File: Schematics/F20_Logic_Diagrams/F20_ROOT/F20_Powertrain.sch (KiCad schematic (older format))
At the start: 1 part, among them U1 Fan

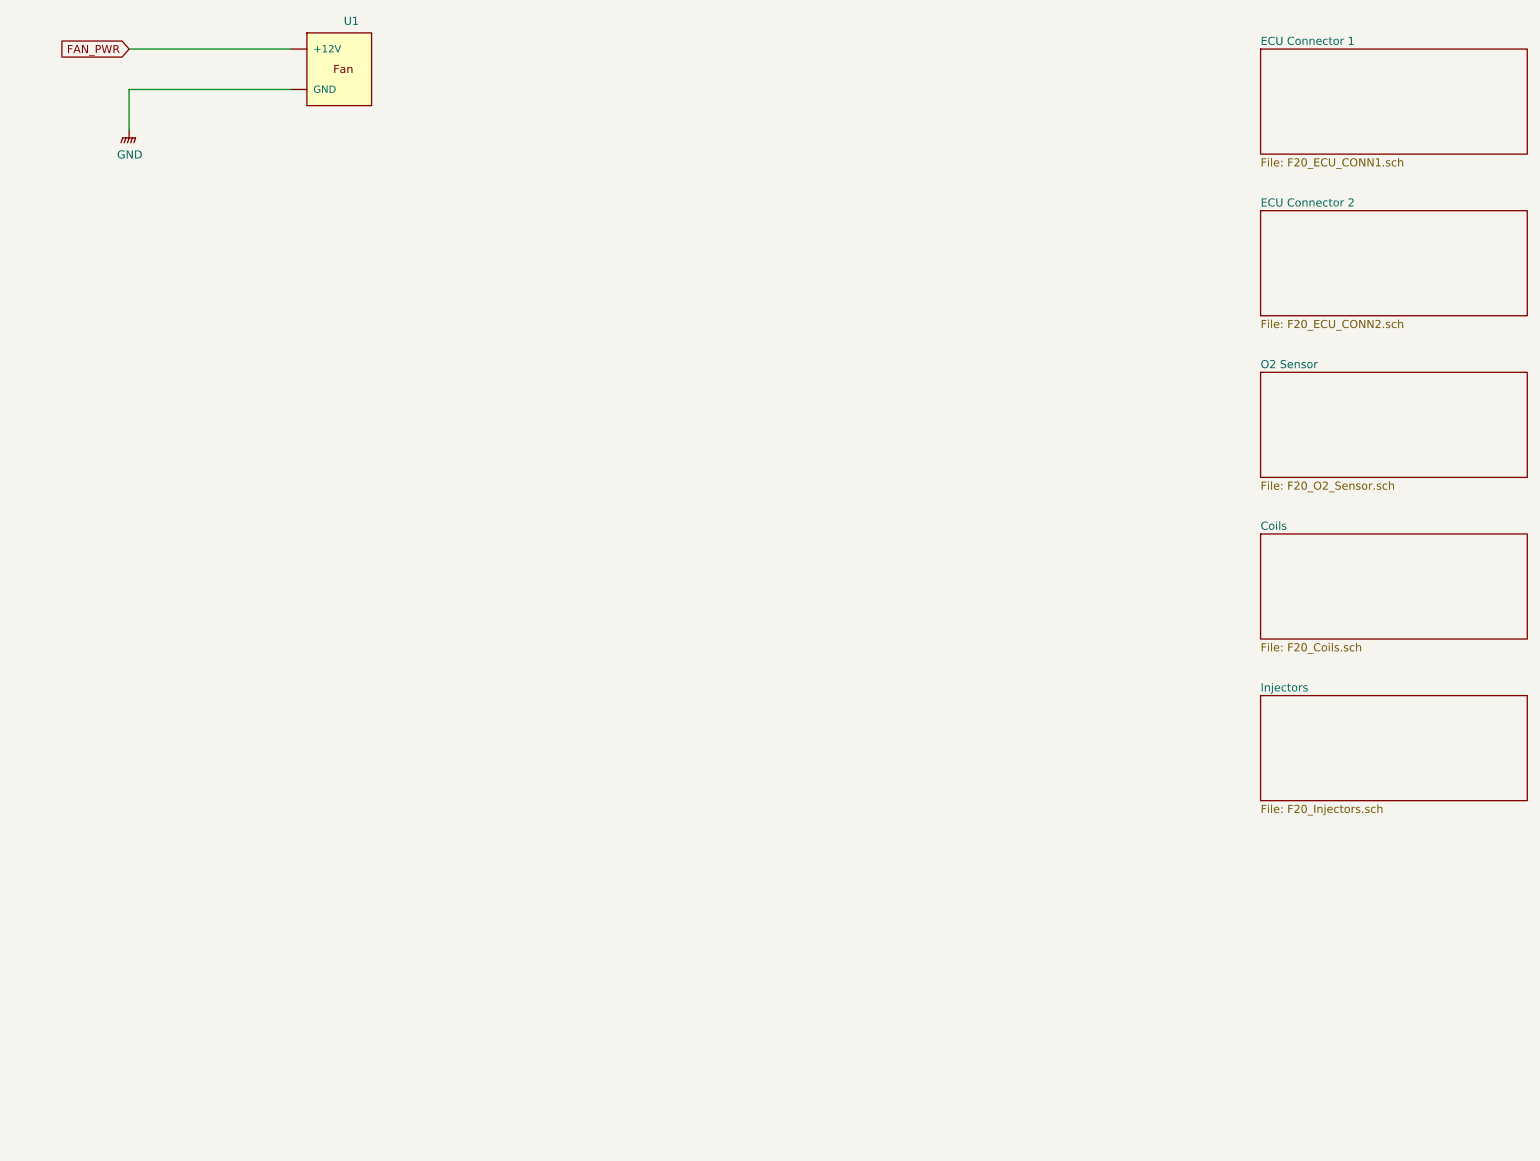
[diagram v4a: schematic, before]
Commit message: Major powertrain update, added shifting schematic
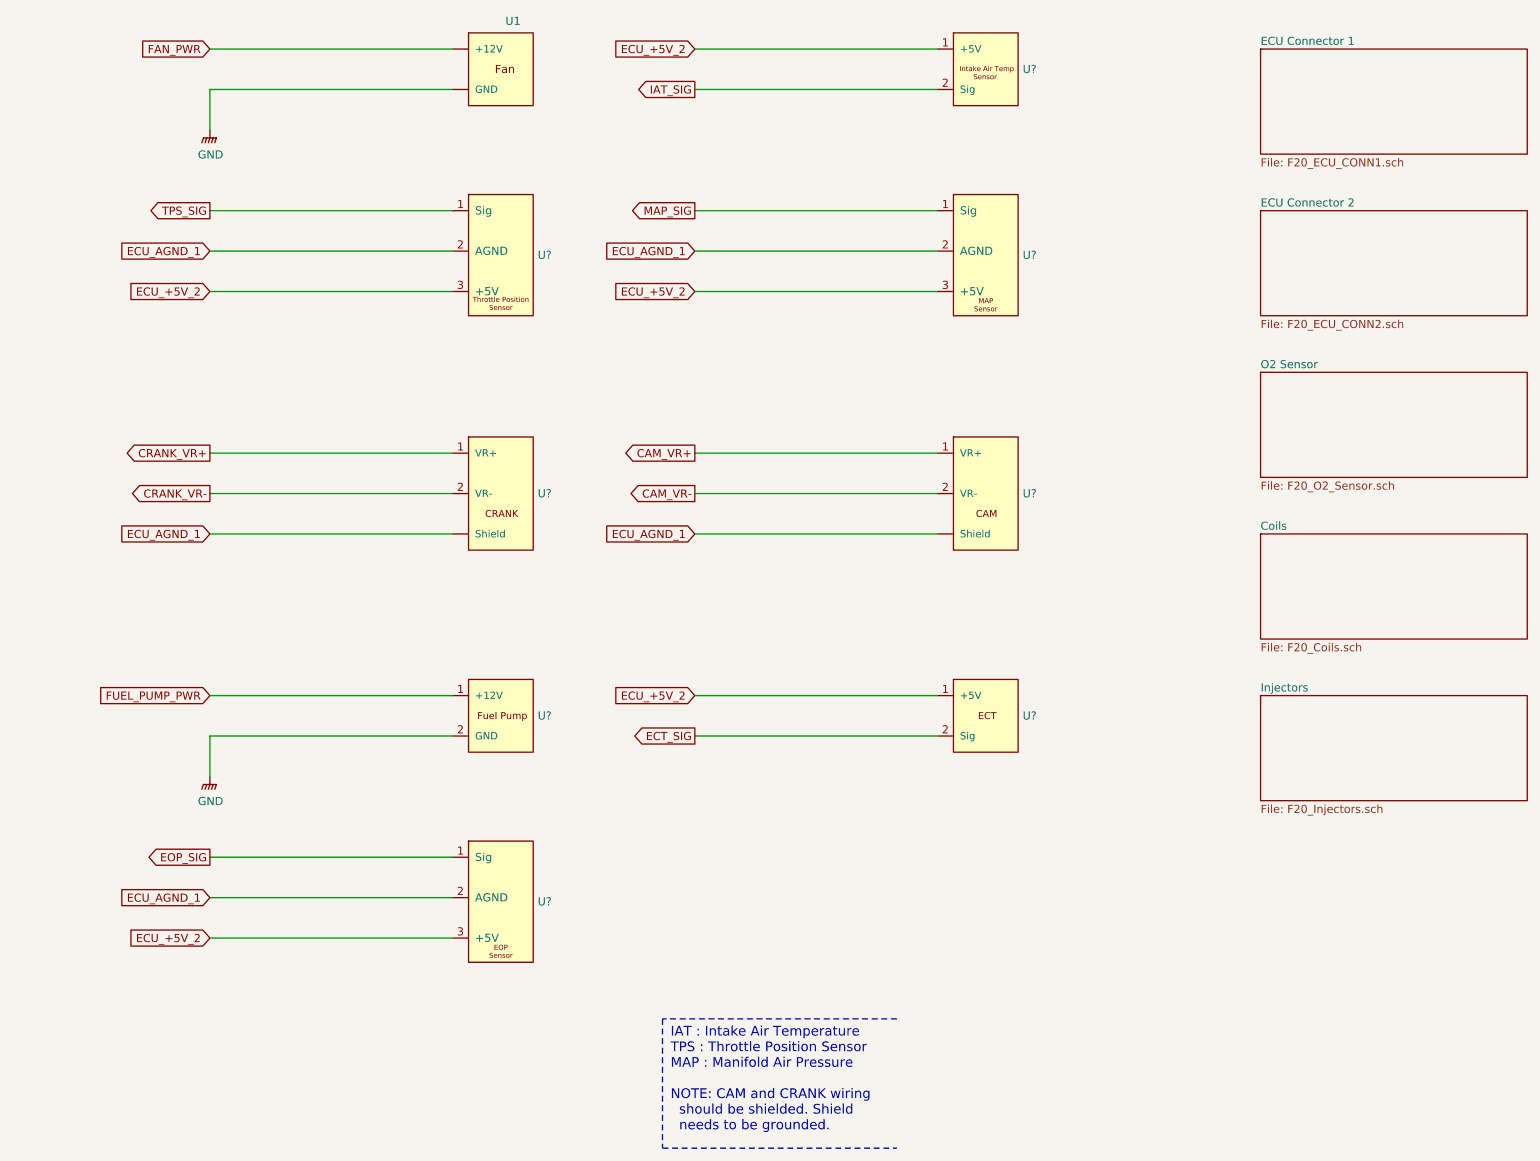
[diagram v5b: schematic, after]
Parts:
- added U?: Fuel_Pump, symbol FSAE_Library:Fuel_Pump
- added U?: Intake_Air_Temp, symbol FSAE_Library:Intake_Air_Temp
- added U?: Throttle_Position_Sensor, symbol FSAE_Library:Throttle_Position_Sensor
- added U?: MAP_Sensor, symbol FSAE_Library:MAP_Sensor
- added U?: Camshaft_Sensor, symbol FSAE_Library:Camshaft_Sensor
- added U?: Crankshaft_Sensor, symbol FSAE_Library:Crankshaft_Sensor
- added U?: ECT_Sensor, symbol FSAE_Library:ECT_Sensor
- added U?: EOP_Sensor, symbol FSAE_Library:EOP_Sensor
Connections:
- net GNDPWR: now also U?.2 (GND)
- new net CAM_VR+: U?.1 (VR+)
- new net CAM_VR-: U?.2 (VR-)
- new net CRANK_VR+: U?.1 (VR+)
- new net CRANK_VR-: U?.2 (VR-)
- new net ECT_SIG: U?.2 (Sig)
- new net ECU_+5V_2: U?.1 (+5V), U?.1 (+5V), U?.3 (+5V), U?.3 (+5V), U?.3 (+5V)
- new net ECU_AGND_1: U?.2 (AGND), U?.2 (AGND), U?.2 (AGND), U?.~ (Shield), U?.~ (Shield)
- new net EOP_SIG: U?.1 (Sig)
- new net FUEL_PUMP_PWR: U?.1 (+12V)
- new net IAT_SIG: U?.2 (Sig)
- new net MAP_SIG: U?.1 (Sig)
- new net TPS_SIG: U?.1 (Sig)
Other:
- note added: "IAT : Intake Air Temperature\nTPS : Throttle Position Sensor\nMAP : Manifold Air Pressure\n\nNOTE: CAM and CRANK wiring\n should be shielded. Shield\n needs to be grounded."
- moved on the sheet: U1
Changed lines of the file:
@@
 $Descr A 11000 8500
 encoding utf-8
-Sheet 2 14
+Sheet 2 15
 Title "Engine"
-Date "2020-02-03"
+Date "2020-03-03"
 Rev "A"
 Comp "F20"
-Comment1 "Cristian Valadez"
+Comment1 "Cristian Valadez, Alex Domagala"
 Comment2 ""
 Comment3 ""
@@
 L FSAE_Library:Fan U1
 U 1 1 5E3D2712
-P 2500 1000
-F 0 "U1" H 2875 1173 50  0000 C CNN
-F 1 "Fan" H 2750 1150 50  0001 C CNN
-F 2 "" H 3000 1500 50  0001 C CNN
-F 3 "" H 3000 1500 50  0001 C CNN
-	1    2500 1000
+P 3500 1000
+F 0 "U1" H 3875 1173 50  0000 C CNN
+F 1 "Fan" H 3750 1150 50  0001 C CNN
+F 2 "" H 4000 1500 50  0001 C CNN
+F 3 "" H 4000 1500 50  0001 C CNN
+	1    3500 1000
 	1    0    0    -1
 $EndComp
@@
 L FSAE_Library:GND #PWR01
 U 1 1 5E3D3AE8
-P 1500 1500
-F 0 "#PWR01" H 1500 1300 50  0001 C CNN
-F 1 "GND" H 1504 1346 50  0000 C CNN
-F 2 "" H 1500 1450 50  0001 C CNN
-F 3 "" H 1500 1450 50  0001 C CNN
-	1    1500 1500
-	1    0    0    -1
-$EndComp
-Wire Wire Line
-	1500 1500 1500 1250
-Wire Wire Line
-	1500 1250 2500 1250
-Text GLabel 1500 1000 0    50   Input ~ 0
+P 2000 1500
+F 0 "#PWR01" H 2000 1300 50  0001 C CNN
+F 1 "GND" H 2004 1346 50  0000 C CNN
+F 2 "" H 2000 1450 50  0001 C CNN
+F 3 "" H 2000 1450 50  0001 C CNN
+	1    2000 1500
+	1    0    0    -1
+$EndComp
+Wire Wire Line
+	2000 1500 2000 1250
+Wire Wire Line
+	2000 1250 3500 1250
+Text GLabel 2000 1000 0    50   Input ~ 0
 FAN_PWR
 Wire Wire Line
-	1500 1000 2500 1000
+	2000 1000 3500 1000
 $Sheet
 S 8500 3000 1650 650
@@
 F1 "F20_Injectors.sch" 50
 $EndSheet
+$Comp
+L FSAE_Library:Fuel_Pump U?
+U 1 1 5E5FB918
+P 3500 5000
+AR Path="/5E5F0904/5E5FB918" Ref="U?"  Part="1"
+AR Path="/5E1D1B45/5E5FB918" Ref="U?"  Part="1"
+F 0 "U?" H 4028 4875 50  0000 L CNN
+F 1 "Fuel_Pump" H 3750 5150 50  0001 C CNN
+F 2 "" H 4000 5500 50  0001 C CNN
+F 3 "" H 4000 5500 50  0001 C CNN
+	1    3500 5000
+	1    0    0    -1
+$EndComp
+Wire Wire Line
+	3500 5000 2000 5000
+Wire Wire Line
+	3500 5250 2000 5250
+Wire Wire Line
+	2000 5250 2000 5500
+$Comp
+L FSAE_Library:GND #PWR?
+U 1 1 5E5FB922
+P 2000 5500
+AR Path="/5E5F0904/5E5FB922" Ref="#PWR?"  Part="1"
+AR Path="/5E1D1B45/5E5FB922" Ref="#PWR?"  Part="1"
+F 0 "#PWR?" H 2000 5300 50  0001 C CNN
+F 1 "GND" H 2004 5346 50  0000 C CNN
+F 2 "" H 2000 5450 50  0001 C CNN
+F 3 "" H 2000 5450 50  0001 C CNN
+	1    2000 5500
+	1    0    0    -1
+$EndComp
+$Comp
+L FSAE_Library:Intake_Air_Temp U?
+U 1 1 5E5FB938
+P 6500 1000
+AR Path="/5E5F0904/5E5FB938" Ref="U?"  Part="1"
+AR Path="/5E1D1B45/5E5FB938" Ref="U?"  Part="1"
+F 0 "U?" H 7028 875 50  0000 L CNN
+F 1 "Intake_Air_Temp" H 6750 1150 50  0001 C CNN
+F 2 "" H 7000 1500 50  0001 C CNN
+F 3 "" H 7000 1500 50  0001 C CNN
+	1    6500 1000
+	1    0    0    -1
+$EndComp
+Wire Wire Line
+	6500 1000 5000 1000
+Wire Wire Line
+	6500 1250 5000 1250
+Text GLabel 5000 1250 0    50   Output ~ 0
+IAT_SIG
+$Comp
+L FSAE_Library:Throttle_Position_Sensor U?
+U 1 1 5E5FB942
+P 3500 2000
+AR Path="/5E5F0904/5E5FB942" Ref="U?"  Part="1"
+AR Path="/5E1D1B45/5E5FB942" Ref="U?"  Part="1"
+F 0 "U?" H 4028 1725 50  0000 L CNN
+F 1 "Throttle_Position_Sensor" H 3800 2150 50  0001 C CNN
+F 2 "" H 4000 2500 50  0001 C CNN
+F 3 "" H 4000 2500 50  0001 C CNN
+	1    3500 2000
+	1    0    0    -1
+$EndComp
+Text GLabel 2000 2500 0    50   Input ~ 0
+ECU_+5V_2
+Wire Wire Line
+	3500 2500 2000 2500
+Wire Wire Line
+	3500 2250 2000 2250
+Text GLabel 2000 2250 0    50   Input ~ 0
+ECU_AGND_1
+Wire Wire Line
+	3500 2000 2000 2000
+Text GLabel 2000 2000 0    50   Output ~ 0
+TPS_SIG
+$Comp
+L FSAE_Library:MAP_Sensor U?
+U 1 1 5E5FB94E
+P 6500 2000
+AR Path="/5E5F0904/5E5FB94E" Ref="U?"  Part="1"
+AR Path="/5E1D1B45/5E5FB94E" Ref="U?"  Part="1"
+F 0 "U?" H 7028 1725 50  0000 L CNN
+F 1 "MAP_Sensor" H 6800 2150 50  0001 C CNN
+F 2 "" H 7000 2500 50  0001 C CNN
+F 3 "" H 7000 2500 50  0001 C CNN
+	1    6500 2000
+	1    0    0    -1
+$EndComp
+Wire Wire Line
+	6500 2000 5000 2000
+Wire Wire Line
+	6500 2250 5000 2250
+Wire Wire Line
+	6500 2500 5000 2500
+Text GLabel 5000 2000 0    50   Output ~ 0
+MAP_SIG
+Text GLabel 5000 2250 0    50   Input ~ 0
+ECU_AGND_1
+Text GLabel 5000 2500 0    50   Input ~ 0
+ECU_+5V_2
+Wire Wire Line
+	3500 3500 2000 3500
+Wire Wire Line
+	3500 4000 2000 4000
+Text GLabel 5000 1000 0    50   Input ~ 0
+ECU_+5V_2
+Text Notes 4850 7700 0    60   ~ 0
+IAT : Intake Air Temperature\nTPS : Throttle Position Sensor\nMAP : Manifold Air Pressure\n\nNOTE: CAM and CRANK wiring\n  should be shielded. Shield\n  needs to be grounded.
+Text GLabel 2000 5000 0    50   Input ~ 0
+FUEL_PUMP_PWR
+Wire Wire Line
+	5000 4000 6500 4000
+Wire Wire Line
+	5000 3500 6500 3500
+Text GLabel 2000 3500 0    50   Output ~ 0
+CRANK_VR+
+Text GLabel 5000 3500 0    50   Output ~ 0
+CAM_VR+
+Wire Notes Line
+	6250 7000 4800 7000
+Wire Notes Line
+	4800 7000 4800 7800
+Wire Notes Line
+	4800 7800 6250 7800
+Text GLabel 2000 4000 0    50   Input ~ 0
+ECU_AGND_1
+Text GLabel 5000 4000 0    50   Input ~ 0
+ECU_AGND_1
+Wire Wire Line
+	3500 3750 2000 3750
+Text GLabel 2000 3750 0    50   Output ~ 0
+CRANK_VR-
+Wire Wire Line
+	6500 3750 5000 3750
+Text GLabel 5000 3750 0    50   Output ~ 0
+CAM_VR-
+$Comp
+L FSAE_Library:Camshaft_Sensor U?
+U 1 1 5E665C35
+P 6500 3500
+F 0 "U?" H 7028 3250 50  0000 L CNN
+F 1 "Camshaft_Sensor" H 6750 3650 50  0001 C CNN
+F 2 "" H 7000 4000 50  0001 C CNN
+F 3 "" H 7000 4000 50  0001 C CNN
+	1    6500 3500
+	1    0    0    -1
+$EndComp
+$Comp
+L FSAE_Library:Crankshaft_Sensor U?
+U 1 1 5E6666BD
+P 3500 3500
+F 0 "U?" H 4028 3250 50  0000 L CNN
+F 1 "Crankshaft_Sensor" H 3750 3650 50  0001 C CNN
+F 2 "" H 4000 4000 50  0001 C CNN
+F 3 "" H 4000 4000 50  0001 C CNN
+	1    3500 3500
+	1    0    0    -1
+$EndComp
+Text GLabel 5000 5250 0    50   Output ~ 0
+ECT_SIG
+Text GLabel 5000 5000 0    50   Input ~ 0
+ECU_+5V_2
+Wire Wire Line
+	5000 5000 6500 5000
+Wire Wire Line
+	6500 5250 5000 5250
+$Comp
+L FSAE_Library:ECT_Sensor U?
+U 1 1 5E695F31
+P 6500 5000
+F 0 "U?" H 7028 4875 50  0000 L CNN
+F 1 "ECT_Sensor" H 6750 5150 50  0001 C CNN
+F 2 "" H 7000 5500 50  0001 C CNN
+F 3 "" H 7000 5500 50  0001 C CNN
+	1    6500 5000
+	1    0    0    -1
+$EndComp
+$Comp
+L FSAE_Library:EOP_Sensor U?
+U 1 1 5E696BEC
+P 3500 6000
+F 0 "U?" H 4028 5725 50  0000 L CNN
+F 1 "EOP_Sensor" H 3800 6150 50  0001 C CNN
+F 2 "" H 4000 6500 50  0001 C CNN
+F 3 "" H 4000 6500 50  0001 C CNN
+	1    3500 6000
+	1    0    0    -1
+$EndComp
+Text GLabel 2000 6500 0    50   Input ~ 0
+ECU_+5V_2
+Wire Wire Line
+	2000 6500 3500 6500
+Text GLabel 2000 6000 0    50   Output ~ 0
+EOP_SIG
+Wire Wire Line
+	2000 6000 3500 6000
+Text GLabel 2000 6250 0    50   Input ~ 0
+ECU_AGND_1
+Wire Wire Line
+	2000 6250 3500 6250
 $EndSCHEMATC
